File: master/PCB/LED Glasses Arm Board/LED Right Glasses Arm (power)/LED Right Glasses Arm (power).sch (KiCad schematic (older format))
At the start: 17 parts, among them Q1 TP0610T, SW1 SW_SPST, U1 TPS63060

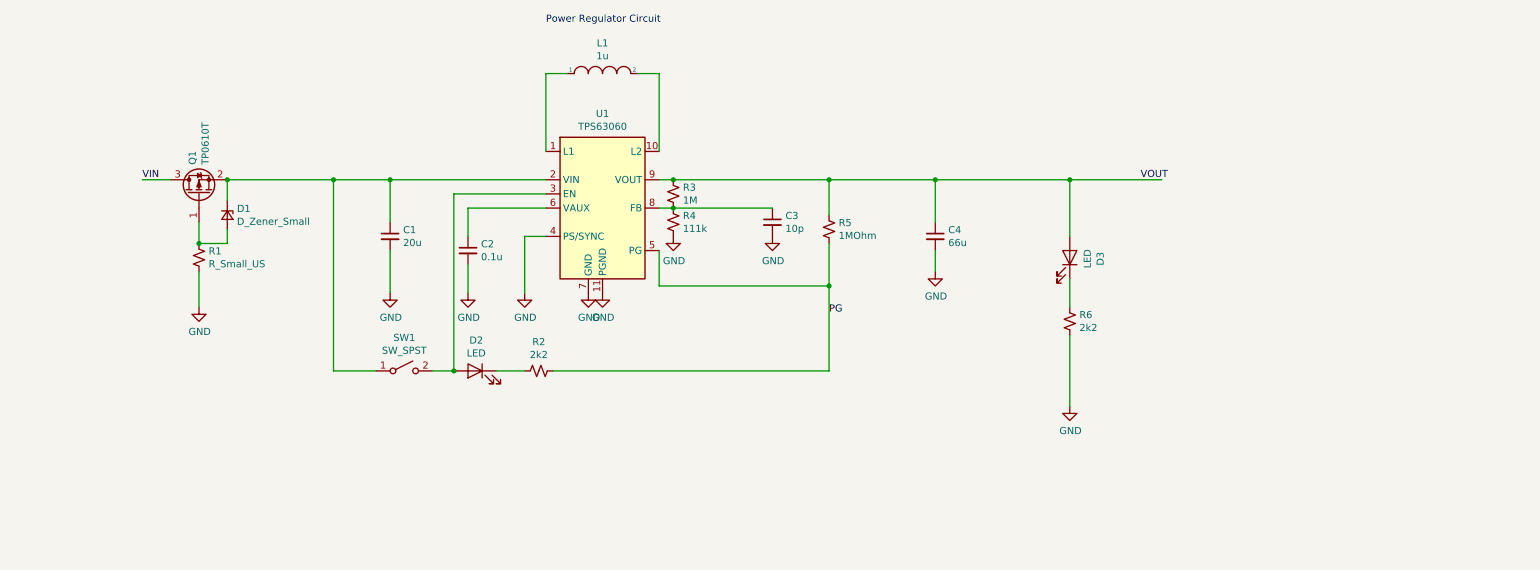
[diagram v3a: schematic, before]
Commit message: Finalising sch and board layout
Added in JST connector for battery pack and pin connectors for the glasses side. Prelim board layout
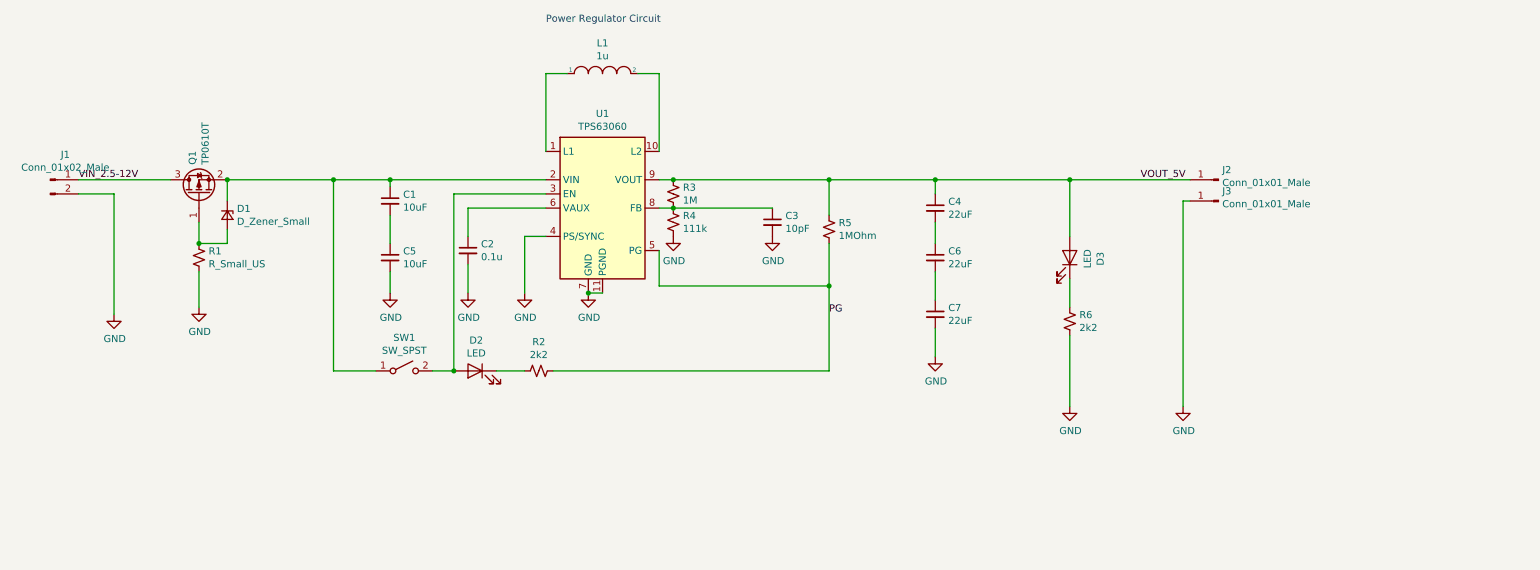
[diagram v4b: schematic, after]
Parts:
- added C5: 10uF, Capacitor_SMD:C_0603_1608Metric, symbol Device:C_Small
- added C6, C7: 22uF, Capacitor_SMD:C_0603_1608Metric, symbol Device:C_Small
- added J1: Conn_01x02_Male, Connector_JST:JST_PH_S2B-PH-K_1x02_P2.00mm_Horizontal, symbol Connector:Conn_01x02_Male
- added J2, J3: Conn_01x01_Male, Connector_PinHeader_1.00mm:PinHeader_1x01_P1.00mm_Vertical_SMD_CUSTOM, symbol Connector:Conn_01x01_Male
- C1: value 20u -> 10uF
- C3: value 10p -> 10pF
- C4: value 66u -> 22uF
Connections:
- net GND: now also C5.2, C7.2, J1.2 (Pin_2), J3.1 (Pin_1); no longer C1.2, C4.2
- net VIN renamed VIN_2.5-12V
- net VIN_2.5-12V: now also J1.1 (Pin_1)
- net VOUT renamed VOUT_5V
- net VOUT_5V: now also J2.1 (Pin_1)
- new net: C1.2, C5.1
- new net: C4.2, C6.1
- new net: C6.2, C7.1
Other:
- moved on the sheet: C1, C4
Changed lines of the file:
@@
 Text Notes 4350 2950 0    50   ~ 0
 Power Regulator Circuit\n
-Text Label 1500 4050 0    50   ~ 0
-VIN
+Text Label 1050 4050 0    50   ~ 0
+VIN_2.5-12V
 Wire Wire Line
 	4350 4450 4200 4450
@@
 $EndComp
 $Comp
-L power:GND #PWR0105
-U 1 1 5F4B6FED
-P 4750 4850
-F 0 "#PWR0105" H 4750 4600 50  0001 C CNN
-F 1 "GND" H 4755 4677 50  0000 C CNN
-F 2 "" H 4750 4850 50  0001 C CNN
-F 3 "" H 4750 4850 50  0001 C CNN
-	1    4750 4850
-	1    0    0    -1
-$EndComp
-$Comp
 L Device:C_Small C1
 U 1 1 5F4B72C8
-P 3250 4450
-F 0 "C1" H 3342 4496 50  0000 L CNN
-F 1 "20u" H 3342 4405 50  0000 L CNN
-F 2 "Capacitor_SMD:C_0603_1608Metric" H 3250 4450 50  0001 C CNN
-F 3 "~" H 3250 4450 50  0001 C CNN
-	1    3250 4450
-	1    0    0    -1
-$EndComp
-Wire Wire Line
-	3250 4350 3250 4050
-Wire Wire Line
-	3250 4550 3250 4850
+P 3250 4200
+F 0 "C1" H 3342 4246 50  0000 L CNN
+F 1 "10uF" H 3342 4155 50  0000 L CNN
+F 2 "Capacitor_SMD:C_0603_1608Metric" H 3250 4200 50  0001 C CNN
+F 3 "~" H 3250 4200 50  0001 C CNN
+	1    3250 4200
+	1    0    0    -1
+$EndComp
 $Comp
 L Device:C_Small C2
@@
 P 5950 4350
 F 0 "C3" H 6042 4396 50  0000 L CNN
-F 1 "10p" H 6042 4305 50  0000 L CNN
+F 1 "10pF" H 6042 4305 50  0000 L CNN
 F 2 "Capacitor_SMD:C_0603_1608Metric" H 5950 4350 50  0001 C CNN
 F 3 "~" H 5950 4350 50  0001 C CNN
@@
 L Device:C_Small C4
 U 1 1 5F4BC943
-P 7100 4450
-F 0 "C4" H 7192 4496 50  0000 L CNN
-F 1 "66u" H 7192 4405 50  0000 L CNN
-F 2 "Capacitor_SMD:C_0603_1608Metric" H 7100 4450 50  0001 C CNN
-F 3 "~" H 7100 4450 50  0001 C CNN
-	1    7100 4450
-	1    0    0    -1
-$EndComp
-Wire Wire Line
-	7100 4350 7100 4050
-Wire Wire Line
-	6350 4050 7100 4050
+P 7100 4250
+F 0 "C4" H 7192 4296 50  0000 L CNN
+F 1 "22uF" H 7192 4205 50  0000 L CNN
+F 2 "Capacitor_SMD:C_0603_1608Metric" H 7100 4250 50  0001 C CNN
+F 3 "~" H 7100 4250 50  0001 C CNN
+	1    7100 4250
+	1    0    0    -1
+$EndComp
 $Comp
 L power:GND #PWR0108
 U 1 1 5F4BEA89
-P 7100 4700
-F 0 "#PWR0108" H 7100 4450 50  0001 C CNN
-F 1 "GND" H 7105 4527 50  0000 C CNN
-F 2 "" H 7100 4700 50  0001 C CNN
-F 3 "" H 7100 4700 50  0001 C CNN
-	1    7100 4700
-	1    0    0    -1
-$EndComp
-Wire Wire Line
-	7100 4550 7100 4700
+P 7100 5300
+F 0 "#PWR0108" H 7100 5050 50  0001 C CNN
+F 1 "GND" H 7105 5127 50  0000 C CNN
+F 2 "" H 7100 5300 50  0001 C CNN
+F 3 "" H 7100 5300 50  0001 C CNN
+	1    7100 5300
+	1    0    0    -1
+$EndComp
 Text Label 8550 4050 0    50   ~ 0
-VOUT
+VOUT_5V
 Connection ~ 6350 4800
 Text Label 6350 5000 0    50   ~ 0
 PG
-Connection ~ 3250 4050
-Wire Wire Line
-	3250 4050 4350 4050
 Wire Wire Line
 	4350 4150 3700 4150
@@
 	2850 5400 2850 4050
 Connection ~ 2850 4050
-Wire Wire Line
-	2850 4050 3250 4050
 $Comp
 L Switch:SW_SPST SW1
@@
 	8050 5150 8050 5650
 Wire Wire Line
-	7100 4050 8050 4050
-Connection ~ 7100 4050
-Wire Wire Line
 	8050 4050 8050 4450
 Connection ~ 8050 4050
-Wire Wire Line
-	8050 4050 8700 4050
 $Comp
 L power:GND #PWR0109
@@
 Wire Wire Line
 	4400 5400 6350 5400
-Wire Wire Line
-	1500 4050 1700 4050
 $Comp
 L Device:D_Zener_Small D1
@@
 	1900 4350 1900 4500
 Connection ~ 1900 4500
+Wire Wire Line
+	4750 4850 4650 4850
+Connection ~ 4650 4850
+$Comp
+L Device:C_Small C5
+U 1 1 604D825D
+P 3250 4600
+F 0 "C5" H 3342 4646 50  0000 L CNN
+F 1 "10uF" H 3342 4555 50  0000 L CNN
+F 2 "Capacitor_SMD:C_0603_1608Metric" H 3250 4600 50  0001 C CNN
+F 3 "~" H 3250 4600 50  0001 C CNN
+	1    3250 4600
+	1    0    0    -1
+$EndComp
+Wire Wire Line
+	2850 4050 3250 4050
+Wire Wire Line
+	3250 4050 3250 4100
+Connection ~ 3250 4050
+Wire Wire Line
+	3250 4050 4350 4050
+Wire Wire Line
+	3250 4300 3250 4500
+Wire Wire Line
+	3250 4700 3250 4850
+Wire Wire Line
+	1050 4050 1700 4050
+Wire Wire Line
+	8050 4050 8900 4050
+$Comp
+L Device:C_Small C7
+U 1 1 604E036B
+P 7100 5000
+F 0 "C7" H 7192 5046 50  0000 L CNN
+F 1 "22uF" H 7192 4955 50  0000 L CNN
+F 2 "Capacitor_SMD:C_0603_1608Metric" H 7100 5000 50  0001 C CNN
+F 3 "~" H 7100 5000 50  0001 C CNN
+	1    7100 5000
+	1    0    0    -1
+$EndComp
+$Comp
+L Device:C_Small C6
+U 1 1 604E0D34
+P 7100 4600
+F 0 "C6" H 7192 4646 50  0000 L CNN
+F 1 "22uF" H 7192 4555 50  0000 L CNN
+F 2 "Capacitor_SMD:C_0603_1608Metric" H 7100 4600 50  0001 C CNN
+F 3 "~" H 7100 4600 50  0001 C CNN
+	1    7100 4600
+	1    0    0    -1
+$EndComp
+Wire Wire Line
+	6350 4050 7100 4050
+Wire Wire Line
+	7100 4050 7100 4150
+Connection ~ 7100 4050
+Wire Wire Line
+	7100 4050 8050 4050
+Wire Wire Line
+	7100 4350 7100 4500
+Wire Wire Line
+	7100 4700 7100 4900
+Wire Wire Line
+	7100 5100 7100 5300
+$Comp
+L Connector:Conn_01x02_Male J1
+U 1 1 604D70E4
+P 850 4050
+F 0 "J1" H 956 4228 50  0000 C CNN
+F 1 "Conn_01x02_Male" H 956 4137 50  0000 C CNN
+F 2 "Connector_JST:JST_PH_S2B-PH-K_1x02_P2.00mm_Horizontal" H 850 4050 50  0001 C CNN
+F 3 "~" H 850 4050 50  0001 C CNN
+	1    850  4050
+	1    0    0    -1
+$EndComp
+Wire Wire Line
+	1050 4150 1300 4150
+Wire Wire Line
+	1300 4150 1300 5000
+$Comp
+L power:GND #PWR0105
+U 1 1 604D7EA7
+P 1300 5000
+F 0 "#PWR0105" H 1300 4750 50  0001 C CNN
+F 1 "GND" H 1305 4827 50  0000 C CNN
+F 2 "" H 1300 5000 50  0001 C CNN
+F 3 "" H 1300 5000 50  0001 C CNN
+	1    1300 5000
+	1    0    0    -1
+$EndComp
+$Comp
+L Connector:Conn_01x01_Male J2
+U 1 1 604D92F9
+P 9100 4050
+F 0 "J2" H 9073 3980 50  0000 R CNN
+F 1 "Conn_01x01_Male" H 9073 4071 50  0000 R CNN
+F 2 "Connector_PinHeader_1.00mm:PinHeader_1x01_P1.00mm_Vertical_SMD_CUSTOM" H 9100 4050 50  0001 C CNN
+F 3 "~" H 9100 4050 50  0001 C CNN
+	1    9100 4050
+	-1   0    0    1
+$EndComp
+$Comp
+L power:GND #PWR0111
+U 1 1 604DB74C
+P 8850 5650
+F 0 "#PWR0111" H 8850 5400 50  0001 C CNN
+F 1 "GND" H 8855 5477 50  0000 C CNN
+F 2 "" H 8850 5650 50  0001 C CNN
+F 3 "" H 8850 5650 50  0001 C CNN
+	1    8850 5650
+	1    0    0    -1
+$EndComp
+$Comp
+L Connector:Conn_01x01_Male J3
+U 1 1 604DC290
+P 9100 4200
+F 0 "J3" H 9073 4130 50  0000 R CNN
+F 1 "Conn_01x01_Male" H 9073 4221 50  0000 R CNN
+F 2 "Connector_PinHeader_1.00mm:PinHeader_1x01_P1.00mm_Vertical_SMD_CUSTOM" H 9100 4200 50  0001 C CNN
+F 3 "~" H 9100 4200 50  0001 C CNN
+	1    9100 4200
+	-1   0    0    1
+$EndComp
+Wire Wire Line
+	8900 4200 8850 4200
+Wire Wire Line
+	8850 4200 8850 5650
 $EndSCHEMATC

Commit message: sch revs
added 1000uF cap, slide switch and changed caps to parallel. need to change mosfet and do footprint for cap
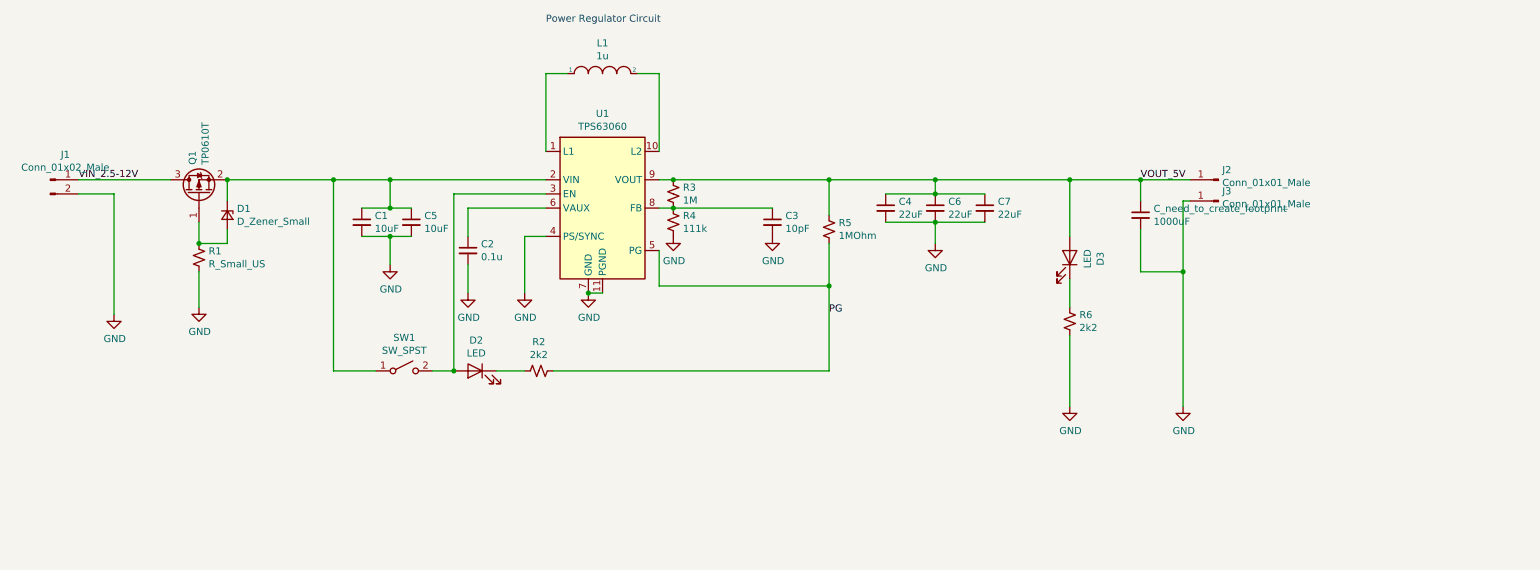
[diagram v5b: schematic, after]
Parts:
- added C_need_to_create_footprint: 1000uF, Capacitor_SMD:C_0603_1608Metric, symbol Device:C_Small
- SW1: footprint Button_Switch_SMD:SW_SPST_FSMSM -> digikey-footprints:Switch_Slide_JS202011SCQN; Digikey Link (none) -> https://www.digikey.com.au/product-detail/en/c-k/JS202011SC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
- U1: footprint Package_SON:Texas_S-PWSON-N10_ThermalVias -> Package_SON:Texas_S-PWSON-N10
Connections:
- net GND: now also C1.2, C4.2, C6.2, C_need_to_create_footprint.2
- net VOUT_5V: now also C6.1, C7.1, C_need_to_create_footprint.1
- net at C1.1, D1.1 (K), Q1.2 (S)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: now also C5.1
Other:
- moved on the sheet: C1, C4, C5, C6, C7
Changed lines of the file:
@@
-$EndComp
-$Comp
-L power:GND #PWR0103
-U 1 1 5F4B6F97
-P 3250 4850
-F 0 "#PWR0103" H 3250 4600 50  0001 C CNN
-F 1 "GND" H 3255 4677 50  0000 C CNN
-F 2 "" H 3250 4850 50  0001 C CNN
-F 3 "" H 3250 4850 50  0001 C CNN
-	1    3250 4850
-	1    0    0    -1
 $EndComp
 $Comp
@@
 L Device:C_Small C1
 U 1 1 5F4B72C8
-P 3250 4200
-F 0 "C1" H 3342 4246 50  0000 L CNN
-F 1 "10uF" H 3342 4155 50  0000 L CNN
-F 2 "Capacitor_SMD:C_0603_1608Metric" H 3250 4200 50  0001 C CNN
-F 3 "~" H 3250 4200 50  0001 C CNN
-	1    3250 4200
+P 3050 4350
+F 0 "C1" H 3142 4396 50  0000 L CNN
+F 1 "10uF" H 3142 4305 50  0000 L CNN
+F 2 "Capacitor_SMD:C_0603_1608Metric" H 3050 4350 50  0001 C CNN
+F 3 "~" H 3050 4350 50  0001 C CNN
+	1    3050 4350
 	1    0    0    -1
 $EndComp
@@
 F 0 "U1" H 4750 4917 50  0000 C CNN
 F 1 "TPS63060" H 4750 4826 50  0000 C CNN
-F 2 "Package_SON:Texas_S-PWSON-N10_ThermalVias" H 4750 3600 50  0001 C CNN
+F 2 "Package_SON:Texas_S-PWSON-N10" H 4750 3600 50  0001 C CNN
 F 3 "http://www.ti.com/lit/ds/symlink/tps63060.pdf" H 4750 4250 50  0001 C CNN
 	1    4750 4250
@@
 L Device:C_Small C4
 U 1 1 5F4BC943
-P 7100 4250
-F 0 "C4" H 7192 4296 50  0000 L CNN
-F 1 "22uF" H 7192 4205 50  0000 L CNN
-F 2 "Capacitor_SMD:C_0603_1608Metric" H 7100 4250 50  0001 C CNN
-F 3 "~" H 7100 4250 50  0001 C CNN
-	1    7100 4250
+P 6750 4250
+F 0 "C4" H 6842 4296 50  0000 L CNN
+F 1 "22uF" H 6842 4205 50  0000 L CNN
+F 2 "Capacitor_SMD:C_0603_1608Metric" H 6750 4250 50  0001 C CNN
+F 3 "~" H 6750 4250 50  0001 C CNN
+	1    6750 4250
 	1    0    0    -1
 $EndComp
@@
 L power:GND #PWR0108
 U 1 1 5F4BEA89
-P 7100 5300
-F 0 "#PWR0108" H 7100 5050 50  0001 C CNN
-F 1 "GND" H 7105 5127 50  0000 C CNN
-F 2 "" H 7100 5300 50  0001 C CNN
-F 3 "" H 7100 5300 50  0001 C CNN
-	1    7100 5300
+P 7100 4500
+F 0 "#PWR0108" H 7100 4250 50  0001 C CNN
+F 1 "GND" H 7105 4327 50  0000 C CNN
+F 2 "" H 7100 4500 50  0001 C CNN
+F 3 "" H 7100 4500 50  0001 C CNN
+	1    7100 4500
 	1    0    0    -1
 $EndComp
@@
 F 0 "SW1" H 3350 5635 50  0000 C CNN
 F 1 "SW_SPST" H 3350 5544 50  0000 C CNN
-F 2 "Button_Switch_SMD:SW_SPST_FSMSM" H 3350 5400 50  0001 C CNN
-F 3 "" H 3350 5400 50  0001 C CNN
+F 2 "digikey-footprints:Switch_Slide_JS202011SCQN" H 3350 5400 50  0001 C CNN
+F 3 "https://www.ckswitches.com/media/1422/js.pdf" H 3350 5400 50  0001 C CNN
+F 4 "https://www.digikey.com.au/product-detail/en/c-k/JS202011SCQN/401-2002-1-ND/1640098" H 3350 5400 50  0001 C CNN "Digikey Link"
 	1    3350 5400
 	1    0    0    -1
@@
 L Device:C_Small C5
 U 1 1 604D825D
-P 3250 4600
-F 0 "C5" H 3342 4646 50  0000 L CNN
-F 1 "10uF" H 3342 4555 50  0000 L CNN
-F 2 "Capacitor_SMD:C_0603_1608Metric" H 3250 4600 50  0001 C CNN
-F 3 "~" H 3250 4600 50  0001 C CNN
-	1    3250 4600
-	1    0    0    -1
-$EndComp
-Wire Wire Line
-	2850 4050 3250 4050
-Wire Wire Line
-	3250 4050 3250 4100
-Connection ~ 3250 4050
-Wire Wire Line
-	3250 4050 4350 4050
-Wire Wire Line
-	3250 4300 3250 4500
-Wire Wire Line
-	3250 4700 3250 4850
+P 3400 4350
+F 0 "C5" H 3492 4396 50  0000 L CNN
+F 1 "10uF" H 3492 4305 50  0000 L CNN
+F 2 "Capacitor_SMD:C_0603_1608Metric" H 3400 4350 50  0001 C CNN
+F 3 "~" H 3400 4350 50  0001 C CNN
+	1    3400 4350
+	1    0    0    -1
+$EndComp
 Wire Wire Line
 	1050 4050 1700 4050
 Wire Wire Line
-	8050 4050 8900 4050
+	8050 4050 8550 4050
 $Comp
 L Device:C_Small C7
 U 1 1 604E036B
-P 7100 5000
-F 0 "C7" H 7192 5046 50  0000 L CNN
-F 1 "22uF" H 7192 4955 50  0000 L CNN
-F 2 "Capacitor_SMD:C_0603_1608Metric" H 7100 5000 50  0001 C CNN
-F 3 "~" H 7100 5000 50  0001 C CNN
-	1    7100 5000
+P 7450 4250
+F 0 "C7" H 7542 4296 50  0000 L CNN
+F 1 "22uF" H 7542 4205 50  0000 L CNN
+F 2 "Capacitor_SMD:C_0603_1608Metric" H 7450 4250 50  0001 C CNN
+F 3 "~" H 7450 4250 50  0001 C CNN
+	1    7450 4250
 	1    0    0    -1
 $EndComp
@@
 L Device:C_Small C6
 U 1 1 604E0D34
-P 7100 4600
-F 0 "C6" H 7192 4646 50  0000 L CNN
-F 1 "22uF" H 7192 4555 50  0000 L CNN
-F 2 "Capacitor_SMD:C_0603_1608Metric" H 7100 4600 50  0001 C CNN
-F 3 "~" H 7100 4600 50  0001 C CNN
-	1    7100 4600
+P 7100 4250
+F 0 "C6" H 7192 4296 50  0000 L CNN
+F 1 "22uF" H 7192 4205 50  0000 L CNN
+F 2 "Capacitor_SMD:C_0603_1608Metric" H 7100 4250 50  0001 C CNN
+F 3 "~" H 7100 4250 50  0001 C CNN
+	1    7100 4250
 	1    0    0    -1
 $EndComp
@@
 Wire Wire Line
 	7100 4350 7100 4500
-Wire Wire Line
-	7100 4700 7100 4900
-Wire Wire Line
-	7100 5100 7100 5300
 $Comp
 L Connector:Conn_01x02_Male J1
@@
 	8900 4200 8850 4200
 Wire Wire Line
-	8850 4200 8850 5650
+	8850 4200 8850 4700
+Wire Wire Line
+	3050 4250 3250 4250
+Connection ~ 3250 4250
+Wire Wire Line
+	3250 4250 3400 4250
+Wire Wire Line
+	2850 4050 3250 4050
+Wire Wire Line
+	3050 4450 3250 4450
+$Comp
+L power:GND #PWR0103
+U 1 1 5F4B6F97
+P 3250 4650
+F 0 "#PWR0103" H 3250 4400 50  0001 C CNN
+F 1 "GND" H 3255 4477 50  0000 C CNN
+F 2 "" H 3250 4650 50  0001 C CNN
+F 3 "" H 3250 4650 50  0001 C CNN
+	1    3250 4650
+	1    0    0    -1
+$EndComp
+Wire Wire Line
+	3250 4050 3250 4250
+Connection ~ 3250 4050
+Wire Wire Line
+	3250 4050 4350 4050
+Wire Wire Line
+	3250 4450 3250 4650
+Connection ~ 3250 4450
+Wire Wire Line
+	3250 4450 3400 4450
+Wire Wire Line
+	6750 4350 7100 4350
+Connection ~ 7100 4350
+Wire Wire Line
+	7100 4350 7450 4350
+Wire Wire Line
+	6750 4150 7100 4150
+Connection ~ 7100 4150
+Wire Wire Line
+	7100 4150 7450 4150
+$Comp
+L Device:C_Small C_need_to_create_footprint
+U 1 1 60505078
+P 8550 4300
+F 0 "C_need_to_create_footprint" H 8642 4346 50  0000 L CNN
+F 1 "1000uF" H 8642 4255 50  0000 L CNN
+F 2 "Capacitor_SMD:C_0603_1608Metric" H 8550 4300 50  0001 C CNN
+F 3 "https://www.vishay.com/docs/40012/591d.pdf" H 8550 4300 50  0001 C CNN
+F 4 "https://www.digikey.com.au/product-detail/en/vishay-sprague/591D108X96R3R2T20H/718-1619-1-ND/1973897" H 8550 4300 50  0001 C CNN "Link"
+	1    8550 4300
+	1    0    0    -1
+$EndComp
+Wire Wire Line
+	8550 4200 8550 4050
+Connection ~ 8550 4050
+Wire Wire Line
+	8550 4050 8900 4050
+Wire Wire Line
+	8550 4400 8550 4700
+Wire Wire Line
+	8550 4700 8850 4700
+Connection ~ 8850 4700
+Wire Wire Line
+	8850 4700 8850 5650
 $EndSCHEMATC
